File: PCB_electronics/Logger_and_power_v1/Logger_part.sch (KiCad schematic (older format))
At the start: 24 parts, among them P10 CONN_01X08, P11 CONN_01X08, P12 CONN_01X03, P13 CONN_01X02, P14 CONN_01X02, P15 CONN_01X02, P5 GPS_breakout_connector, P6 SD_breakout_connector, P7 Iridium_connector, P8 VN100_connector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

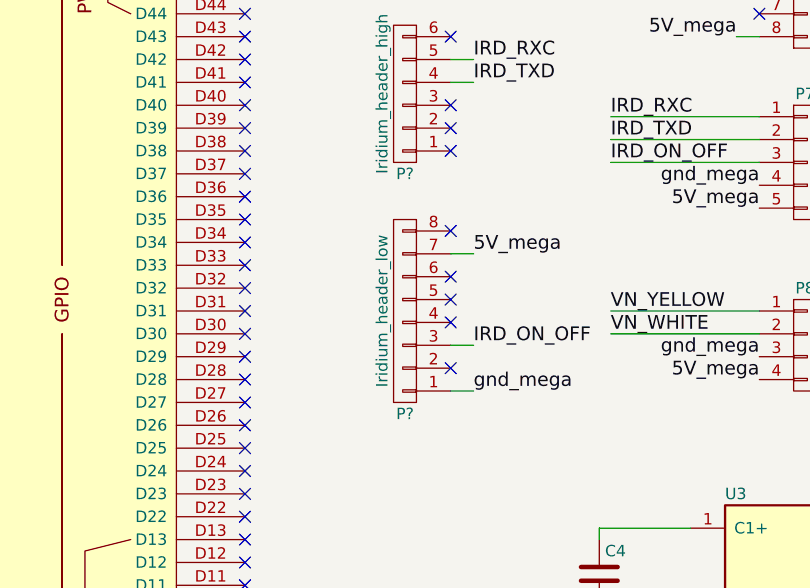
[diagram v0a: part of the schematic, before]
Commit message: corrected shape of the board; added missing wire
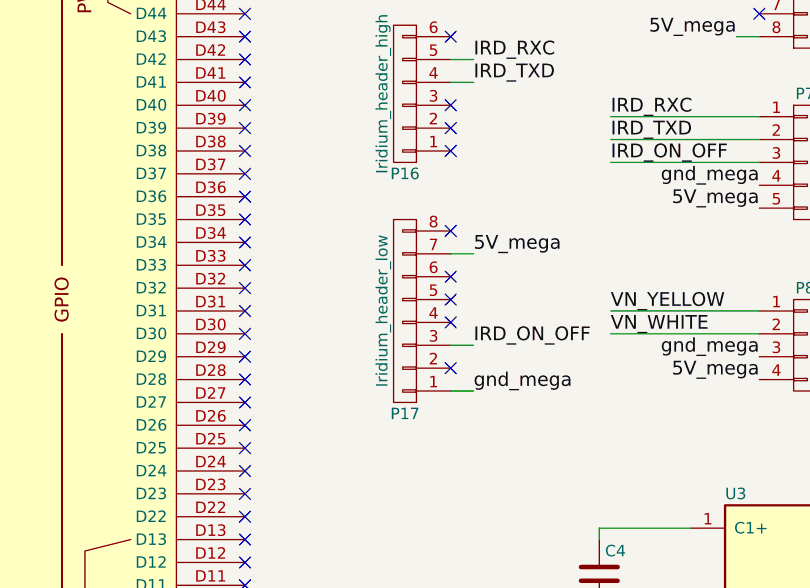
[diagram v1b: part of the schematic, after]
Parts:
- P16: renamed from P?; footprint (none) -> Pin_Headers:Pin_Header_Straight_1x06
- P17: renamed from P?; footprint (none) -> Pin_Headers:Pin_Header_Straight_1x08
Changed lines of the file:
@@
 $EndComp
 $Comp
-L CONN_01X06 P?
+L CONN_01X06 P16
 U 1 1 5B0BCC6F
 P 4600 2850
-F 0 "P?" H 4600 3200 50  0000 C CNN
+F 0 "P16" H 4600 3200 50  0000 C CNN
 F 1 "Iridium_header_high" V 4700 2850 50  0000 C CNN
-F 2 "" H 4600 2850 50  0000 C CNN
+F 2 "Pin_Headers:Pin_Header_Straight_1x06" H 4600 2850 50  0001 C CNN
 F 3 "" H 4600 2850 50  0000 C CNN
 	1    4600 2850
@@
 $EndComp
 $Comp
-L CONN_01X08 P?
+L CONN_01X08 P17
 U 1 1 5B0BD29B
 P 4600 3800
-F 0 "P?" H 4600 4250 50  0000 C CNN
+F 0 "P17" H 4600 4250 50  0000 C CNN
 F 1 "Iridium_header_low" V 4700 3800 50  0000 C CNN
-F 2 "" H 4600 3800 50  0000 C CNN
+F 2 "Pin_Headers:Pin_Header_Straight_1x08" H 4600 3800 50  0001 C CNN
 F 3 "" H 4600 3800 50  0000 C CNN
 	1    4600 3800

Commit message: just commit to work further
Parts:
- U3: value MAX232 -> MAX3323E
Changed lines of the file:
@@
 P 6450 5450
 F 0 "U3" H 6000 6300 50  0000 L CNN
-F 1 "MAX232" H 6650 6300 50  0000 L CNN
+F 1 "MAX3323E" H 6650 6300 50  0000 L CNN
 F 2 "Housings_DIP:DIP-16_W7.62mm_LongPads" H 6450 5450 50  0001 C CNN
 F 3 "" H 6450 5450 50  0000 C CNN

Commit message: working on the pcb v3.5
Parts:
- C4, C5, C6, C7: value 1.0uF -> 100nF
- R8: value 46k -> 47k
- R9: value 32k -> 47k
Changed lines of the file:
@@
 P 7700 2650
 F 0 "R8" V 7780 2650 50  0000 C CNN
-F 1 "46k" V 7700 2650 50  0000 C CNN
+F 1 "47k" V 7700 2650 50  0000 C CNN
 F 2 "Resistors_ThroughHole:Resistor_Horizontal_RM10mm" V 7630 2650 50  0001 C CNN
 F 3 "" H 7700 2650 50  0000 C CNN
@@
 P 8050 3700
 F 0 "R9" V 8130 3700 50  0000 C CNN
-F 1 "32k" V 8050 3700 50  0000 C CNN
+F 1 "47k" V 8050 3700 50  0000 C CNN
 F 2 "Resistors_ThroughHole:Resistor_Horizontal_RM10mm" V 7980 3700 50  0001 C CNN
 F 3 "" H 8050 3700 50  0000 C CNN
@@
 P 5450 4950
 F 0 "C4" H 5475 5050 50  0000 L CNN
-F 1 "1.0uF" H 5475 4850 50  0000 L CNN
+F 1 "100nF" H 5475 4850 50  0000 L CNN
 F 2 "Capacitors_ThroughHole:C_Disc_D3_P2.5" H 5488 4800 50  0001 C CNN
 F 3 "" H 5450 4950 50  0000 C CNN
@@
 P 5450 5450
 F 0 "C5" H 5475 5550 50  0000 L CNN
-F 1 "1.0uF" H 5475 5350 50  0000 L CNN
+F 1 "100nF" H 5475 5350 50  0000 L CNN
 F 2 "Capacitors_ThroughHole:C_Disc_D3_P2.5" H 5488 5300 50  0001 C CNN
 F 3 "" H 5450 5450 50  0000 C CNN
@@
 P 7400 5150
 F 0 "C6" H 7425 5250 50  0000 L CNN
-F 1 "1.0uF" V 7250 5050 50  0000 L CNN
+F 1 "100nF" V 7250 5050 50  0000 L CNN
 F 2 "Capacitors_ThroughHole:C_Disc_D3_P2.5" H 7438 5000 50  0001 C CNN
 F 3 "" H 7400 5150 50  0000 C CNN
@@
 P 7400 5650
 F 0 "C7" H 7425 5750 50  0000 L CNN
-F 1 "1.0uF" V 7250 5550 50  0000 L CNN
+F 1 "100nF" V 7250 5550 50  0000 L CNN
 F 2 "Capacitors_ThroughHole:C_Disc_D3_P2.5" H 7438 5500 50  0001 C CNN
 F 3 "" H 7400 5650 50  0000 C CNN
